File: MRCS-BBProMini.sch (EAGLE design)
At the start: 10 parts, among them J1 2.1mm

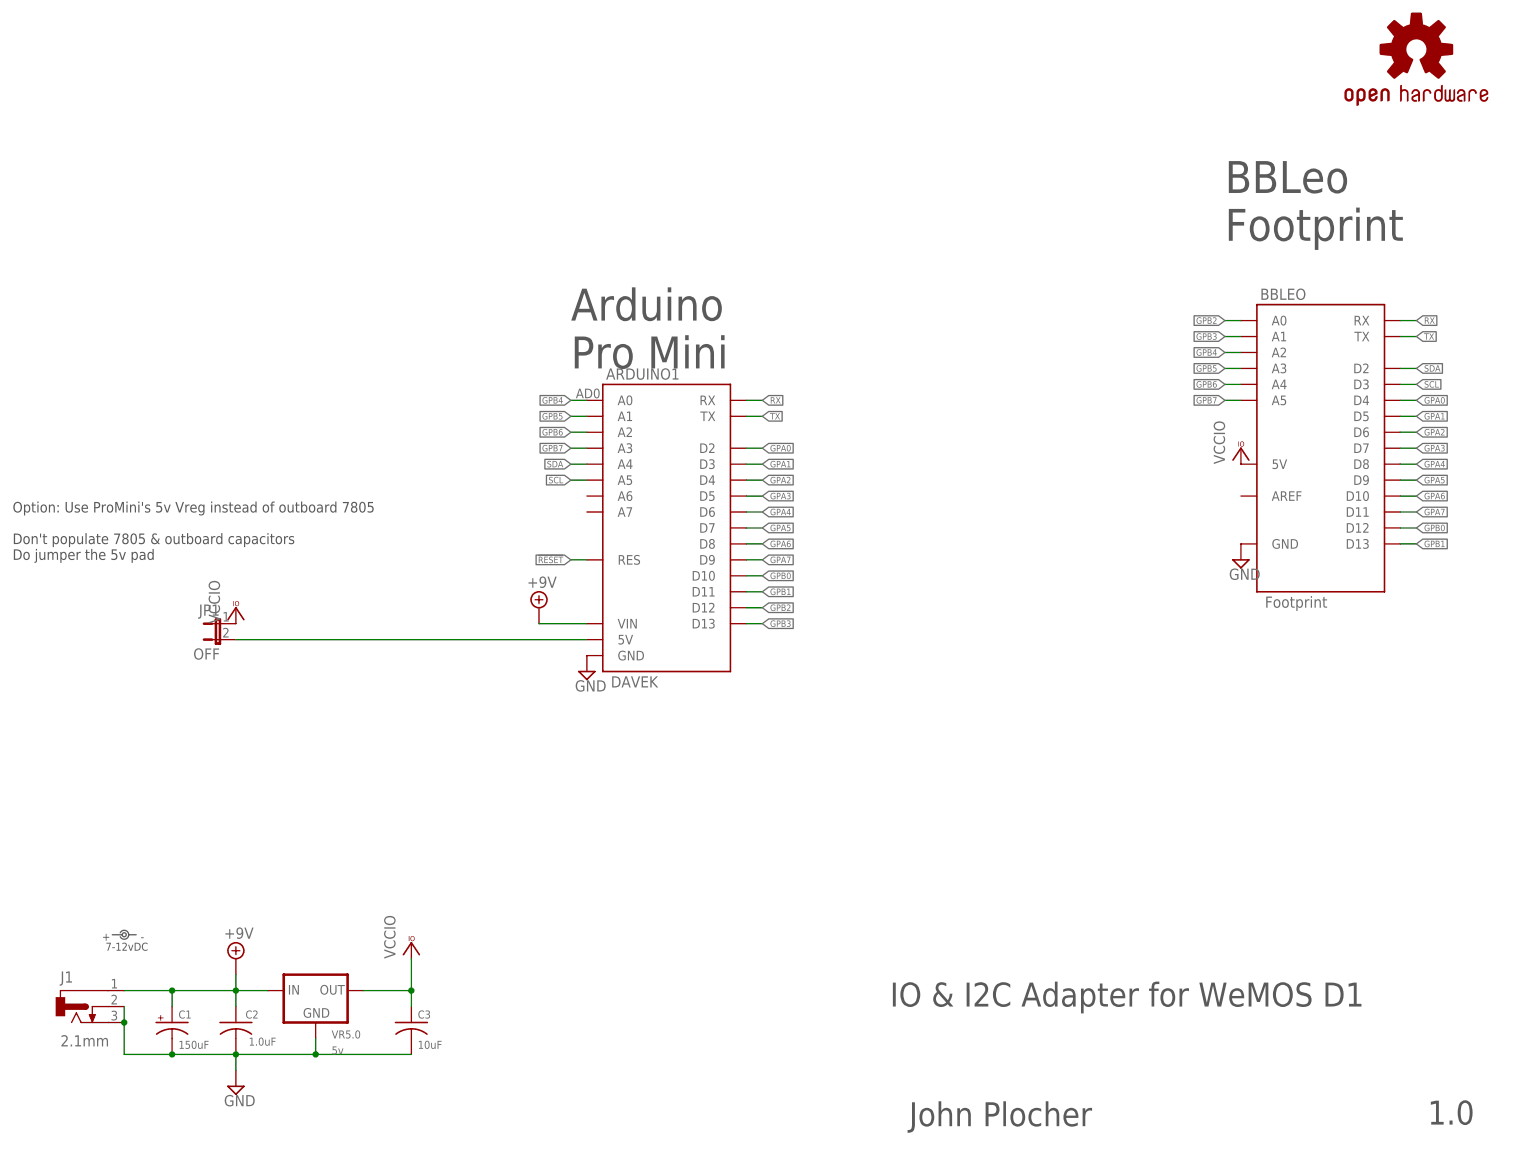
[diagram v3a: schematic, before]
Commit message: Add 2k2 pullup to pin13
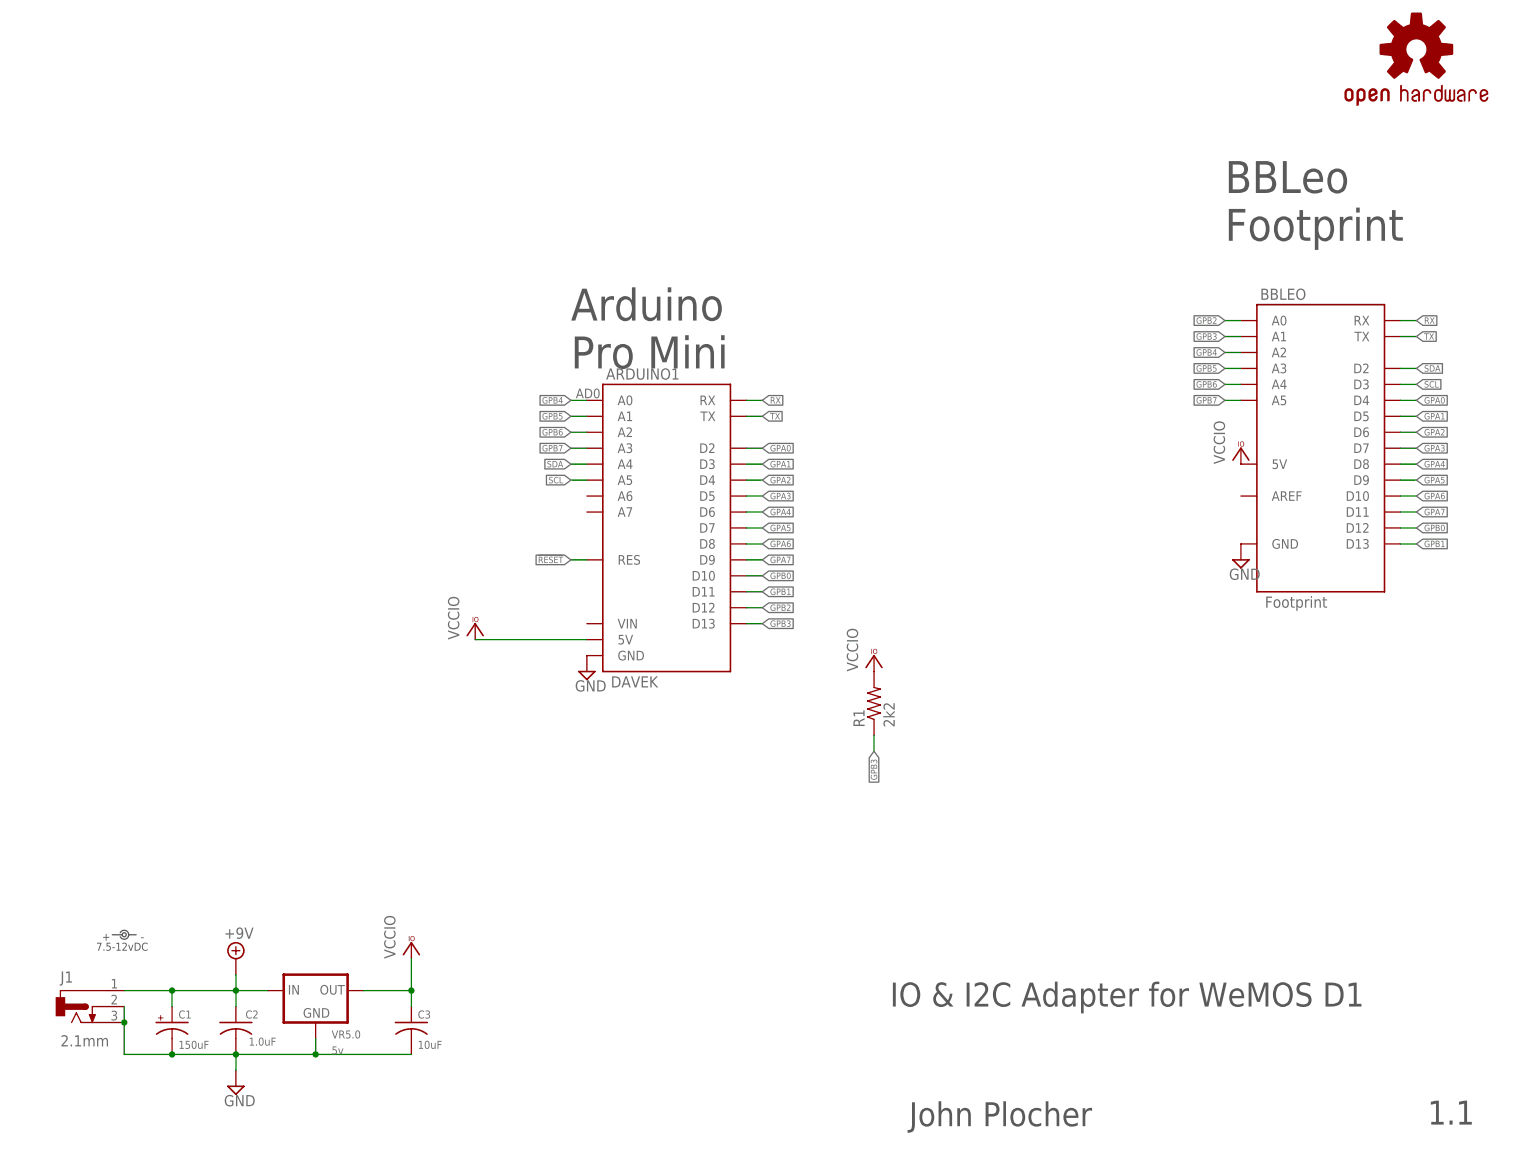
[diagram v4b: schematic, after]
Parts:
- removed JP1: OFF, SPCoast:JUMPER-2SMD-NO
- added R1: 2k2, SPCoast:RPTH03
- LABEL1: value 7-12vDC -> 7.5-12vDC
- VR5.0: device SPCoast:VREG-PTH-RA-5 -> SPCoast:VREG-PTH-RA-
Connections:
- removed net N$1: ARDUINO1.5V, JP1.2
- net +9V: no longer ARDUINO1.VIN
- net GPB3: now also R1.1
- net VCCIO: now also ARDUINO1.5V, R1.2; no longer JP1.1
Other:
- note added: "1.1"
- note added: "Pins A6, A7 and GND on end of board are not used"
- note added: "V1.1 - Add 2k2 pullup on pin13 to counteract the pulldown of builtin LED"
- note removed: "1.0"
- note removed: "Option: Use ProMini's 5v Vreg instead of outboard 7805 Don't populate 7805 & outboard capacitors Do jumper the 5v pad"
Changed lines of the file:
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@@
 <layer number="255" name="routoute" color="7" fill="1" visible="yes" active="yes"/>
 </layers>
-<schematic xreflabel="%F%N/%S.%C%R" xrefpart="/%S.%C%R">
+<schematic xreflabel="%F%N/%S" xrefpart="/%S.%C%R">
 <attributes>
 </attributes>
@@
 <part name="V12" library="supply2" deviceset="GND" device=""/>
 <part name="J1" library="SPCoast" deviceset="CONNECTOR-DC-POWER" device="-RA" value="2.1mm"/>
-<part name="LABEL1" library="SPCoast" deviceset="DOC-POWER_LABEL" device="" value="7-12vDC"/>
+<part name="LABEL1" library="SPCoast" deviceset="DOC-POWER_LABEL" device="" value="7.5-12vDC"/>
 <part name="C3" library="SPCoast" deviceset="CAP*" device="PTH1" value="10uF"/>
 <part name="C2" library="SPCoast" deviceset="CAP*" device="PTH1" value="1.0uF"/>
-<part name="VR5.0" library="SPCoast" deviceset="VREG-?-*" device="PTH-RA" technology="5" value="5v"/>
+<part name="VR5.0" library="SPCoast" deviceset="VREG-?-*" device="PTH-RA" value="5v"/>
 <part name="VCC8" library="supply1" deviceset="VCCIO" device=""/>
 <part name="C1" library="SPCoast" deviceset="CAP-POL*" device="PTH-5MM" value="150uF"/>
@@
 <part name="ARDUINO1" library="SPCoast" deviceset="ARDUINO-PRO-MINI" device="DAVESROBOT" value="DAVEK"/>
 <part name="V1" library="supply2" deviceset="GND" device=""/>
-<part name="SUPPLY1" library="supply2" deviceset="+9V" device=""/>
-<part name="JP1" library="SPCoast" deviceset="JUMPER-2" device="SMD-NO" value="OFF"/>
 <part name="VCC1" library="supply1" deviceset="VCCIO" device=""/>
+<part name="R1" library="SPCoast" deviceset="R*" device="PTH03" value="2k2"/>
+<part name="VCC2" library="supply1" deviceset="VCCIO" device=""/>
 </parts>
 <sheets>
@@
 <text x="149.86" y="25.4" size="3.81" layer="97">IO &amp; I2C Adapter for WeMOS D1</text>
 <text x="152.908" y="6.35" size="3.81" layer="97">John Plocher</text>
-<text x="235.458" y="6.604" size="3.81" layer="97">1.0</text>
-<text x="152.4" y="38.1" size="1.6764" layer="102">Processor carrier board for Daves Robot style Pro Mini</text>
+<text x="235.458" y="6.604" size="3.81" layer="97">1.1</text>
+<text x="142.24" y="38.1" size="1.6764" layer="102">V1.1 - Add 2k2 pullup on pin13 to counteract the pulldown of builtin LED</text>
 <text x="99.06" y="127" size="5.08" layer="97">Arduino
 Pro Mini</text>
 <text x="203.2" y="147.32" size="5.08" layer="97">BBLeo
 Footprint</text>
-<text x="10.16" y="96.52" size="1.6764" layer="97">Option: Use ProMini's 5v Vreg instead of outboard 7805
-Don't populate 7805 &amp; outboard capacitors
-Do jumper the 5v pad </text>
+<text x="142.24" y="40.64" size="1.6764" layer="102">Pins A6, A7 and GND on end of board are not used</text>
+<text x="142.24" y="43.18" size="1.6764" layer="102">Processor carrier board for Daves Robot style Pro Mini</text>
 </plain>
 <instances>
@@
 <instance part="ARDUINO1" gate="A" x="114.3" y="101.6"/>
 <instance part="V1" gate="GND" x="101.6" y="78.74"/>
-<instance part="SUPPLY1" gate="G$1" x="93.98" y="88.9" smashed="yes">
-<attribute name="VALUE" x="92.075" y="92.075" size="1.778" layer="96"/>
-</instance>
-<instance part="JP1" gate="A" x="43.18" y="86.36" rot="MR270"/>
-<instance part="VCC1" gate="G$1" x="45.72" y="88.9"/>
+<instance part="VCC1" gate="G$1" x="83.82" y="86.36"/>
+<instance part="R1" gate="R" x="147.32" y="73.66" rot="R90"/>
+<instance part="VCC2" gate="G$1" x="147.32" y="81.28"/>
 </instances>
 <busses>
@@
 <junction x="35.56" y="27.94"/>
 </segment>
-<segment>
-<pinref part="ARDUINO1" gate="A" pin="VIN"/>
-<pinref part="SUPPLY1" gate="G$1" pin="+9V"/>
-<wire x1="101.6" y1="86.36" x2="93.98" y2="86.36" width="0.1524" layer="91"/>
-</segment>
 </net>
 <net name="SDA" class="2">
@@
 </segment>
 <segment>
-<pinref part="JP1" gate="A" pin="1"/>
+<pinref part="R1" gate="R" pin="2"/>
+<pinref part="VCC2" gate="G$1" pin="VCCIO"/>
+</segment>
+<segment>
+<pinref part="ARDUINO1" gate="A" pin="5V"/>
 <pinref part="VCC1" gate="G$1" pin="VCCIO"/>
+<wire x1="83.82" y1="83.82" x2="101.6" y2="83.82" width="0.1524" layer="91"/>
 </segment>
 </net>
@@
 <pinref part="ARDUINO1" gate="A" pin="D13"/>
 </segment>
+<segment>
+<pinref part="R1" gate="R" pin="1"/>
+<wire x1="147.32" y1="68.58" x2="147.32" y2="66.04" width="0.1524" layer="91"/>
+<label x="147.32" y="66.04" size="1.016" layer="95" rot="R270" xref="yes"/>
+</segment>
 </net>
 <net name="GPB4" class="0">
@@
 </segment>
 </net>
-<net name="N$1" class="0">
-<segment>
-<pinref part="ARDUINO1" gate="A" pin="5V"/>
-<pinref part="JP1" gate="A" pin="2"/>
-<wire x1="101.6" y1="83.82" x2="45.72" y2="83.82" width="0.1524" layer="91"/>
-</segment>
-</net>
